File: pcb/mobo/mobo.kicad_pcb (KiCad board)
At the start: 2 copper layers, 51.6 x 89 mm, 73 parts, among them J1 SWD_10, J2 PEEL_MOTOR, J3 DRIVE_MOTOR, J4 SW1, J5 SPRING_FINGERS, J6 SW2, J7 SW1, J8 USART1, J9 SWD_10, U1 STM32F031C6Tx, U2 STM32F031K6Ux, U4 AP1117-33, U5 MC34063AD, U6 MAX3078E, U7 DRV8837, U8 DRV8837, Y1 8MHz

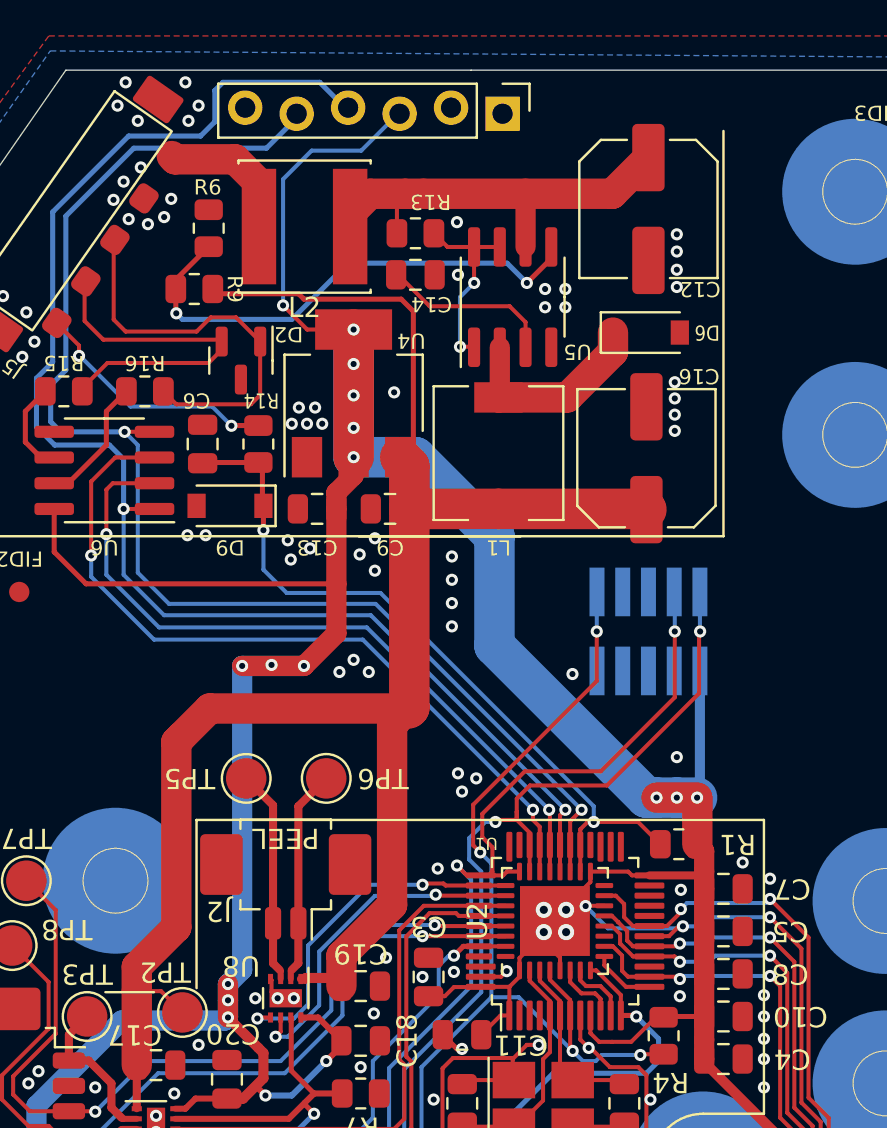
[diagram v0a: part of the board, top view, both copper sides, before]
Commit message: changed C16 footprint and repositioned slightly
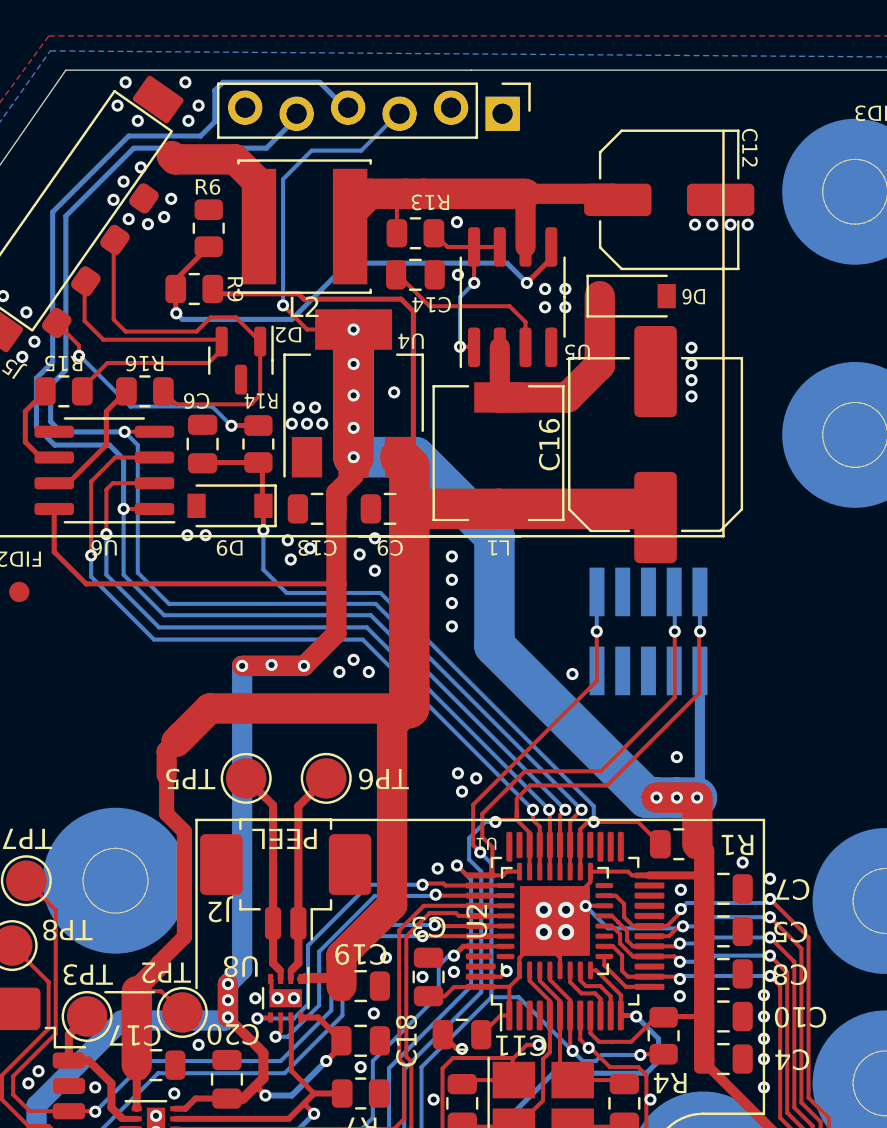
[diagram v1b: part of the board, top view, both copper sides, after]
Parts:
- C16: footprint Capacitor_SMD:C_Elec_6.3x7.7 -> Capacitor_SMD:C_Elec_8x10.2
- moved D6 1.91 mm to (134.8, 41.0)
- moved C12 1.12 mm to (136.6, 36.2), turned to 0 degrees
- moved C16 0.81 mm to (135.9, 48.3)
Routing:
- net +VDC: track 21.3 -> 19.4 mm
- net Net-(D6-K): track 10.0 -> 11.6 mm
- net +10V: track 93.2 -> 93.9 mm
